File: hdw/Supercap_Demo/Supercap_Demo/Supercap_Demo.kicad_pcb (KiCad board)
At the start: 4 copper layers, 71 parts, among them J201 +3.3VIN, J202 VOUT, Q201 IRF7404, Q301 2N7002, Q401 2N7002, U301 LTC3128-UFD, U302 LTC4419DD, U401 LTC3129UD

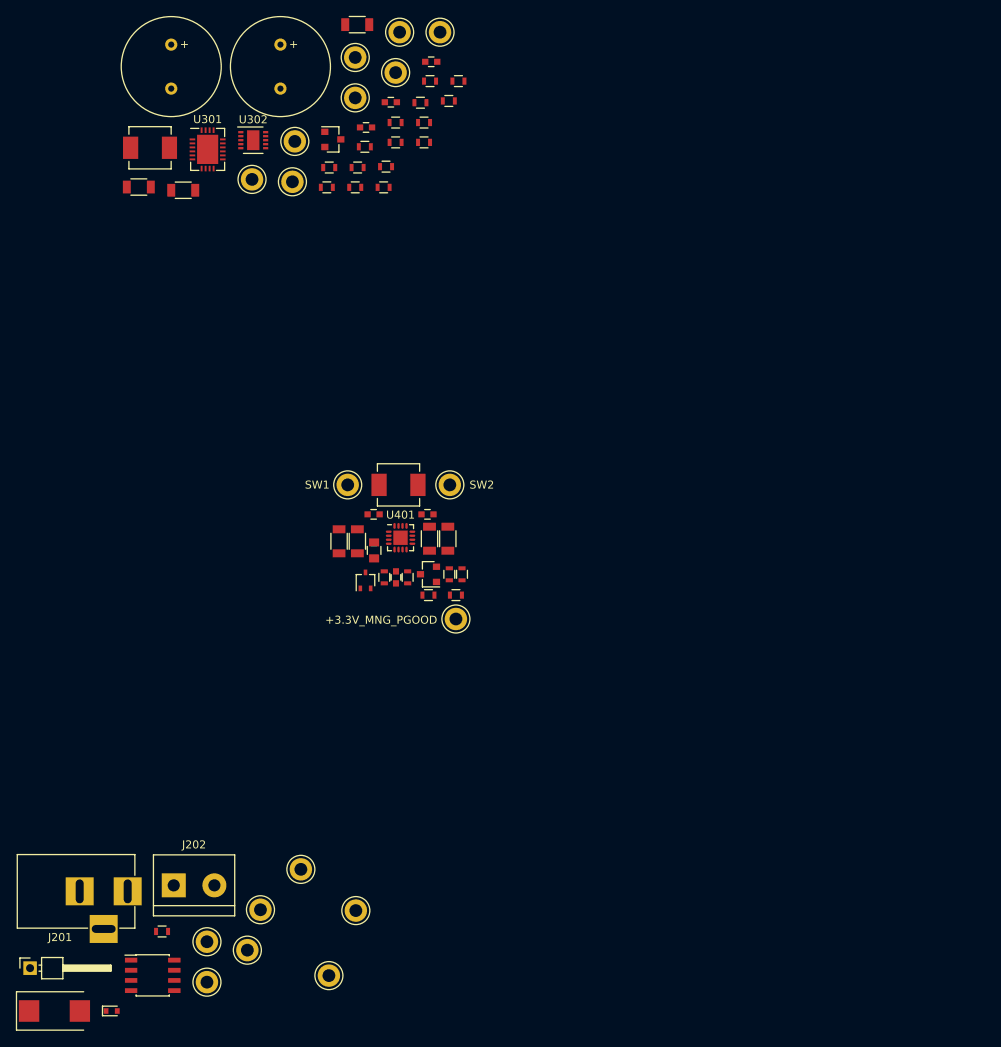
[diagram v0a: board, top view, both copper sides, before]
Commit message: Placed parts on PCB
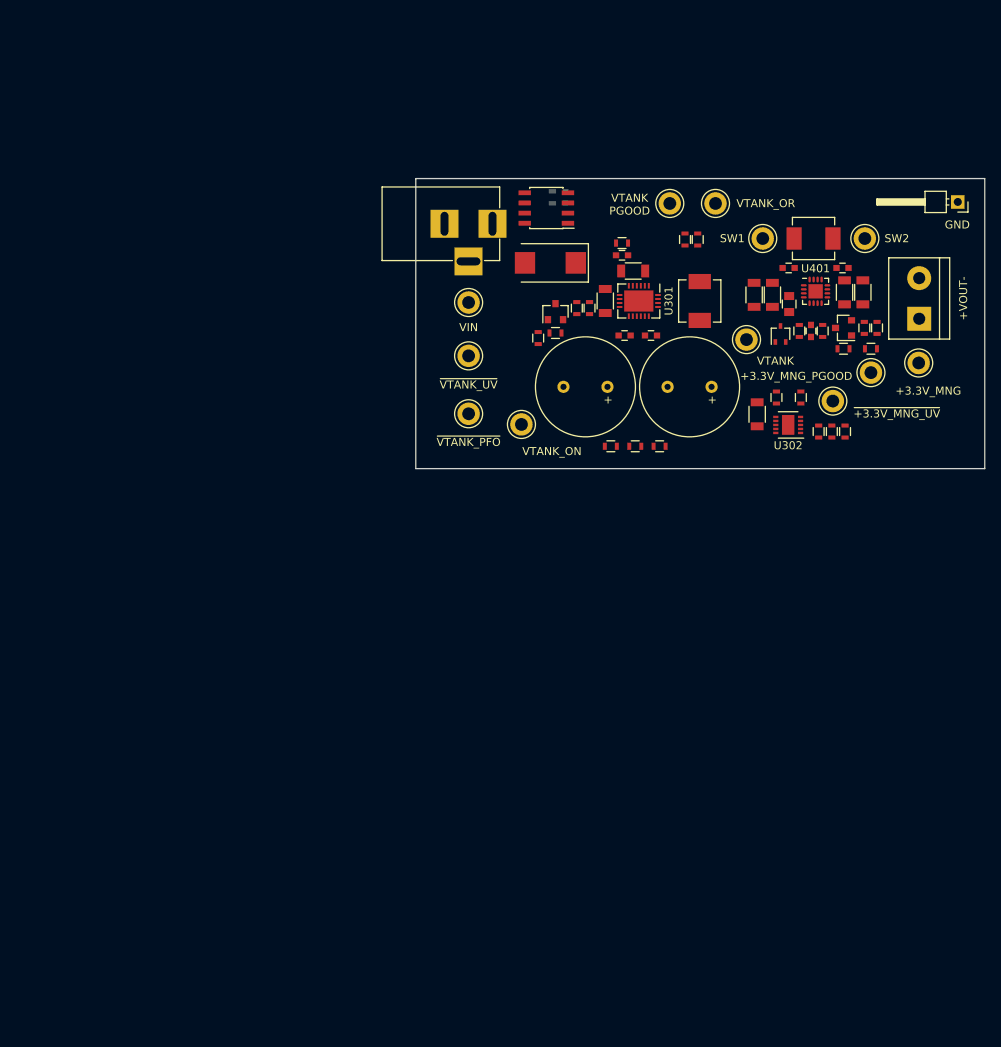
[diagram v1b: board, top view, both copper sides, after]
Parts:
- removed TP301, TP303, TP304, TP305, TP306, TP307: TP, Measurement_Points:Test_Point_Keystone_5005-5009_Compact
- D201, R201: moved to B.Cu
- moved TP202 150.4 mm to (172.0, 29.2), turned to 180 degrees
- moved J202 117.0 mm to (167.1, 43.8), turned to 90 degrees
- moved D201 116.5 mm to (122.9, 28.6), turned to 90 degrees
- moved C201 112.2 mm to (121.0, 36.8), turned to 180 degrees
- moved Q201 107.8 mm to (120.5, 30.0), turned to 180 degrees
- moved TP403 106.3 mm to (167.1, 49.3), turned to 270 degrees
- moved R201 103.9 mm to (121.3, 28.6), turned to 270 degrees
- moved TP201 96.7 mm to (136.0, 29.4), turned to 270 degrees
- moved J201 95.1 mm to (113.8, 31.9)
- moved TP204 88.6 mm to (156.3, 54.1), turned to 270 degrees
- moved TP208 85.5 mm to (110.8, 41.8), turned to 270 degrees
- moved TP206 80.0 mm to (117.4, 57.0), turned to 270 degrees
- moved U302 75.7 mm to (150.7, 57.1), turned to 180 degrees
- moved TP205 74.0 mm to (110.8, 48.5), turned to 270 degrees
- moved TP203 73.7 mm to (110.8, 55.7), turned to 270 degrees
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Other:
- board outline added: 71.1 x 36.3 mm
- board text added: "+3.3V_MNG"
- board text added: "+VOUT-"
- board text added: "GND"
- board text added: "VIN"
- board text added: "VTANK"
- board text added: "VTANK PGOOD"
- board text added: "VTANK_ON"
- board text added: "VTANK_OR"
- board text added: "~+3.3V_MNG_UV"
- board text added: "~VTANK_PFO"
- board text added: "~VTANK_UV"

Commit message: Placed parts on PCB
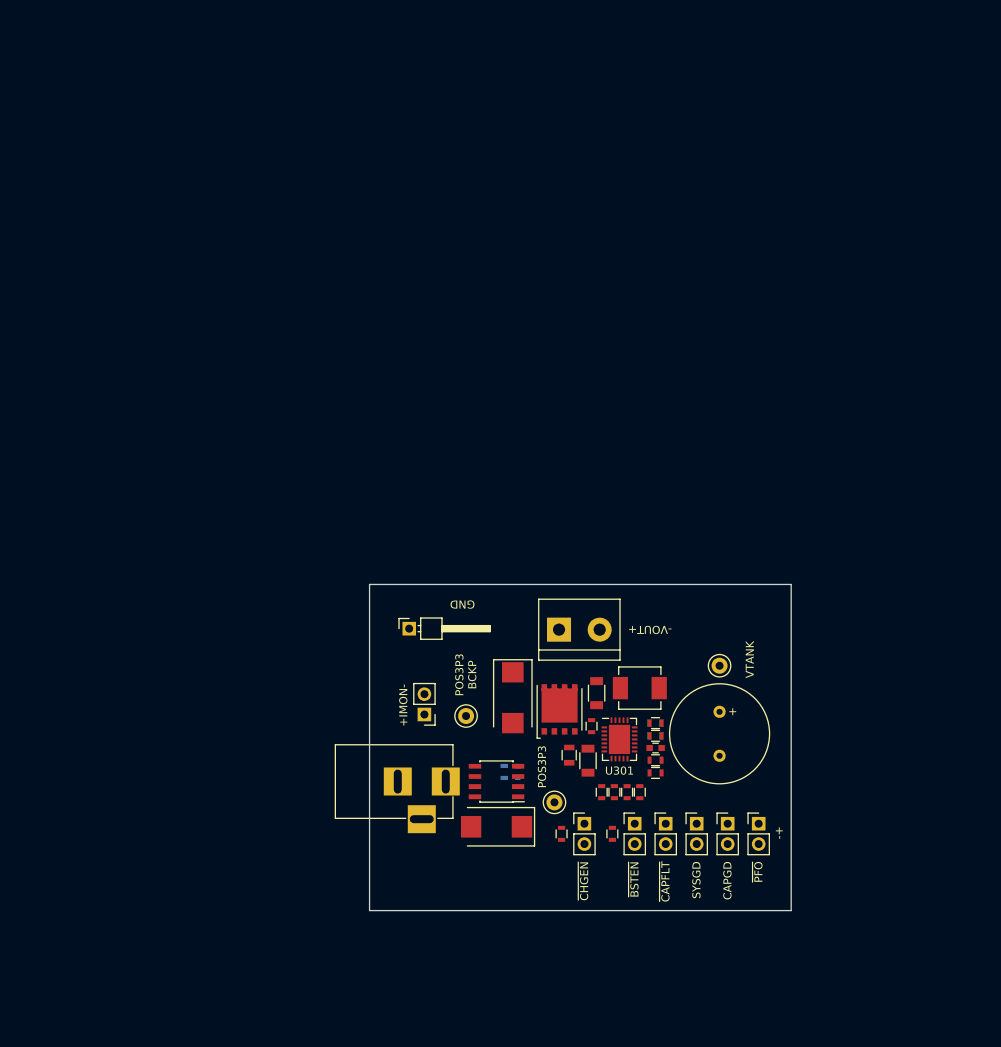
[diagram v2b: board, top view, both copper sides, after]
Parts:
- removed C306: 0.1uF, Capacitors_SMD:C_0603
- removed C307: 470pF, Capacitors_SMD:C_0603
- removed C308, C401, C402, C407, C408: 10uF, Capacitors_SMD:C_1206
- removed C403, C404: 22nF, Capacitors_SMD:C_0603
- removed C405: 2.2uF, Capacitors_SMD:C_0805
- removed C406: 33pF, Capacitors_SMD:C_0603
- removed D401: BAT54W, TO_SOT_Packages_SMD:SOT-323_SC-70
- removed L401: 3.3uH, Inductors_SMD:L_Vishay_IHLP-2020
- removed Q401: 2N7002, TO_SOT_Packages_SMD:SOT-23
- removed R315, R402, R404, R405: 1M, Resistors_SMD:R_0603
- removed R401: 10, Resistors_SMD:R_0603
- removed R403: 100k, Resistors_SMD:R_0603
- removed R406: 1.07M, Resistors_SMD:R_0603
- removed R407: 590k, Resistors_SMD:R_0603
- removed TP203, TP204, TP205, TP206, TP207, TP208, TP308, TP401, TP402, TP403: TP, Measurement_Points:Test_Point_Keystone_5005-5009_Compact
- removed U302: LTC4419DD, Housings_DFN_QFN:DFN-10-1EP_3x3mm_Pitch0.5mm
- removed U401: LTC3129UD, Housings_DFN_QFN:QFN-16-1EP_3x3mm_Pitch0.5mm
- added JP301: ~CHGEN, Pin_Headers:Pin_Header_Straight_1x02_Pitch2.54mm, F.Cu at (125.3, 106.9)
- added JP302: ~BSTEN, Pin_Headers:Pin_Header_Straight_1x02_Pitch2.54mm, F.Cu at (131.6, 106.9)
- added TP301: IMON, Pin_Headers:Pin_Header_Straight_1x02_Pitch2.54mm, F.Cu at (105.3, 93.3)
- added TP303: CAPGD, Pin_Headers:Pin_Header_Straight_1x02_Pitch2.54mm, F.Cu at (143.2, 106.9)
- added TP304: SYSGD, Pin_Headers:Pin_Header_Straight_1x02_Pitch2.54mm, F.Cu at (139.3, 106.9)
- added TP305: PFO, Pin_Headers:Pin_Header_Straight_1x02_Pitch2.54mm, F.Cu at (147.1, 106.9)
- added TP306: TP, Measurement_Points:Test_Point_Keystone_5000-5004_Miniature, F.Cu at (110.5, 93.5)
- added TP307: TP, Measurement_Points:Test_Point_Keystone_5000-5004_Miniature, F.Cu at (142.2, 87.2)
- C302: value 10uF -> 2.2nF; footprint Capacitors_SMD:C_1206 -> Capacitors_SMD:C_0603
- C303: value 15F -> 10uF; footprint Custom Footprints Library:SCCT30B156SRB -> Capacitors_SMD:C_1206
- C305: value 0.1uF -> 100uF; footprint Capacitors_SMD:C_0603 -> Capacitors_Tantalum_SMD:CP_Tantalum_Case-D_EIA-7343-31_Reflow
- L301: value 3.3uH -> 2.2uH
- Q301: value 2N7002 -> IPC100N04S51R7ATMA1; footprint TO_SOT_Packages_SMD:SOT-23 -> TO_SOT_Packages_SMD:TDSON-8-1
- R304: value 124k -> 1M
- R306: value 10 -> 1M
- R307: value 3.6k -> 121k; moved to B.Cu
- R308: value 2.2M -> 75k; moved to B.Cu
- R309: value 3.65k -> 12m; footprint Resistors_SMD:R_0603 -> Resistors_SMD:R_0805
- R310: value 340k -> 1k
- R311: value 1M -> 1.07M
- R312: value 324k -> 340k
- R313: value 276k -> 931k
- R314: value 1M -> 392k
- TP201: footprint Measurement_Points:Test_Point_Keystone_5005-5009_Compact -> Pin_Headers:Pin_Header_Angled_1x01_Pitch2.54mm
- TP202: footprint Pin_Headers:Pin_Header_Angled_1x01_Pitch2.54mm -> Measurement_Points:Test_Point_Keystone_5000-5004_Miniature
- TP302: value TP -> ~CAPFLT; footprint Measurement_Points:Test_Point_Keystone_5005-5009_Compact -> Pin_Headers:Pin_Header_Straight_1x02_Pitch2.54mm
- U301: value LTC3128-UFD -> LTC4041UFD; footprint Housings_DFN_QFN:QFN-20-1EP_4x5mm_Pitch0.5mm -> Housings_DFN_QFN:QFN-24-1EP_4x5mm_Pitch0.5mm
- moved TP202 90.4 mm to (121.5, 104.3), turned to 0 degrees
- moved R201 72.1 mm to (115.3, 100.5)
- moved D201 72.1 mm to (117.0, 100.5)
- moved Q201 72.0 mm to (114.3, 101.7)
- moved C201 70.8 mm to (114.3, 107.3)
- moved J201 70.0 mm to (108.0, 101.7)
- moved R302 69.6 mm to (129.0, 103.0)
- moved R304 65.8 mm to (122.4, 108.2)
- moved R301 65.3 mm to (134.2, 99.0), turned to 180 degrees
- moved R306 62.7 mm to (128.8, 108.2), turned to 90 degrees
- moved TP201 62.3 mm to (103.4, 82.5), turned to 0 degrees
- moved TP302 61.4 mm to (135.4, 106.9), turned to 0 degrees
- moved R307 60.2 mm to (134.2, 94.4), turned to 180 degrees
- moved C302 59.7 mm to (134.2, 97.5), turned to 0 degrees
- moved J202 59.5 mm to (122.1, 82.7), turned to 0 degrees
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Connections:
- C303 pad 1: VTANK -> +3.3V_BCKP
- C303 pad 2: Net-(C303-Pad2) -> GND
- C304 pad 1: Net-(C303-Pad2) -> VTANK
- C305 pad 1: VTANK -> +3.3V_BCKP
- C305 pad 2: Net-(C303-Pad2) -> GND
- J202 pad 1: +3.3V_MNG -> +3.3V_BCKP
- L301 pad 2: Net-(L301-Pad2) -> VTANK
- Q301 pad 2: GND -> Net-(Q301-Pad1)
- Q301 pad 3: Net-(Q301-Pad3) -> Net-(Q301-Pad1)
- R301 pad 1: ~TANK_PFO -> +3.3V_BCKP
- R301 pad 2: +3.3V_MNG -> ~BCKP_PFO
- R302 pad 1: TANK_PGOOD -> +3.3V_BCKP
- R302 pad 2: +3.3V_MNG -> BCKP_SYSGD
- R303 pad 1: Net-(Q301-Pad3) -> +3.3V_BCKP
- R303 pad 2: +3V3 -> BCKP_CAPGD
- R304 pad 1: GND -> +3V3
- R304 pad 2: Net-(R304-Pad2) -> Net-(JP301-Pad1)
- R305 pad 1: GND -> +3.3V_BCKP
- R305 pad 2: Net-(Q301-Pad1) -> ~BCKP_CAPFLT
- R306 pad 1: Net-(Q301-Pad1) -> +3V3
- R306 pad 2: VTANK_ON -> Net-(JP302-Pad1)
- R307 pad 1: GND -> +3V3
- R307 pad 2: Net-(C307-Pad1) -> Net-(R307-Pad2)
- R308 pad 1: Net-(R308-Pad1) -> Net-(R307-Pad2)
- R308 pad 2: VTANK -> GND
- R309 pad 1: Net-(R309-Pad1) -> Net-(Q301-Pad1)
- R309 pad 2: Net-(R308-Pad1) -> +3V3
- R310 pad 1: GND -> Net-(R310-Pad1)
- R310 pad 2: Net-(R309-Pad1) -> GND
- R311 pad 1: Net-(R311-Pad1) -> +3.3V_BCKP
- R311 pad 2: Net-(C302-Pad1) -> Net-(R311-Pad2)
- R312 pad 1: Net-(R312-Pad1) -> Net-(R311-Pad2)
- R312 pad 2: Net-(R311-Pad1) -> GND
- R313 pad 1: GND -> VTANK
- R313 pad 2: Net-(R312-Pad1) -> Net-(R313-Pad2)
- R314 pad 1: ~POS3P3_UV -> Net-(R313-Pad2)
- R314 pad 2: +3.3V_MNG -> GND
- TP201 pad 1: TANK_PGOOD -> GND
- TP202 pad 1: GND -> +3V3
- TP302 pad 1: VTANK -> ~BCKP_CAPFLT
- U301 pad 1: Net-(L301-Pad2) -> +3.3V_BCKP
- U301 pad 10: Net-(R304-Pad2) -> Net-(R311-Pad2)
- U301 pad 11: Net-(R308-Pad1) -> BCKP_SYSGD
- U301 pad 12: TANK_PGOOD -> Net-(R313-Pad2)
- U301 pad 13: Net-(C303-Pad2) -> BCKP_CAPGD
- U301 pad 14: VTANK -> ~BCKP_PFO
- U301 pad 15: VTANK -> Net-(Q301-Pad4)
- U301 pad 16: VTANK -> +3V3
- U301 pad 17: Net-(L301-Pad1) -> Net-(C302-Pad1)
- U301 pad 18: Net-(L301-Pad1) -> Net-(R311-Pad2)
- U301 pad 19: Net-(L301-Pad2) -> Net-(R307-Pad2)
- U301 pad 2: Net-(C302-Pad1) -> Net-(R310-Pad1)
- U301 pad 20: (no net) -> GND
- U301 pad 21: GND -> Net-(L301-Pad1)
- U301 pad 3: Net-(C302-Pad1) -> BCKP_IMON
- U301 pad 4: Net-(Q301-Pad3) -> Net-(JP301-Pad1)
- U301 pad 5: Net-(C307-Pad1) -> Net-(JP302-Pad1)
- U301 pad 6: (no net) -> +3V3
- U301 pad 7: +3V3 -> Net-(Q301-Pad1)
- U301 pad 8: ~TANK_PFO -> ~BCKP_CAPFLT
- U301 pad 9: Net-(Q301-Pad3) -> (no net)
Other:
- board size 71.1 x 36.3 mm -> 52.7 x 40.8 mm
- board text added: "+IMON-"
- board text added: "-+"
- board text added: "-VOUT+"
- board text added: "CAPGD"
- board text added: "POS3P3"
- board text added: "POS3P3 BCKP"
- board text added: "SYSGD"
- board text added: "~BSTEN"
- board text added: "~CAPFLT"
- board text added: "~CHGEN"
- board text added: "~PFO"
- board text removed: "+3.3V_MNG"
- board text removed: "+3.3V_MNG_PGOOD"
- board text removed: "+VOUT-"
- board text removed: "SW1"
- board text removed: "SW2"
- board text removed: "VIN"
- board text removed: "VTANK PGOOD"
- board text removed: "VTANK_ON"
- board text removed: "VTANK_OR"
- board text removed: "~+3.3V_MNG_UV"
- board text removed: "~VTANK_PFO"
- board text removed: "~VTANK_UV"

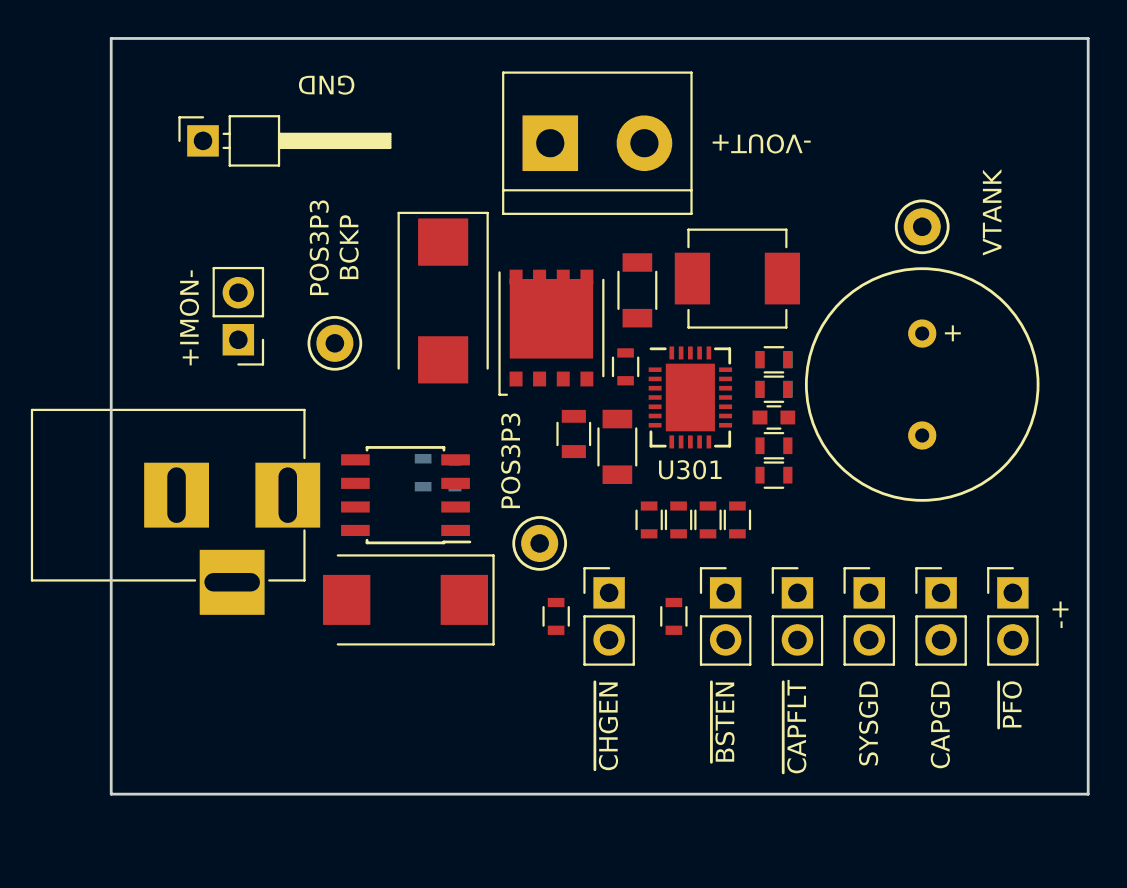
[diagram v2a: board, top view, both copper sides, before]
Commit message: Routed board
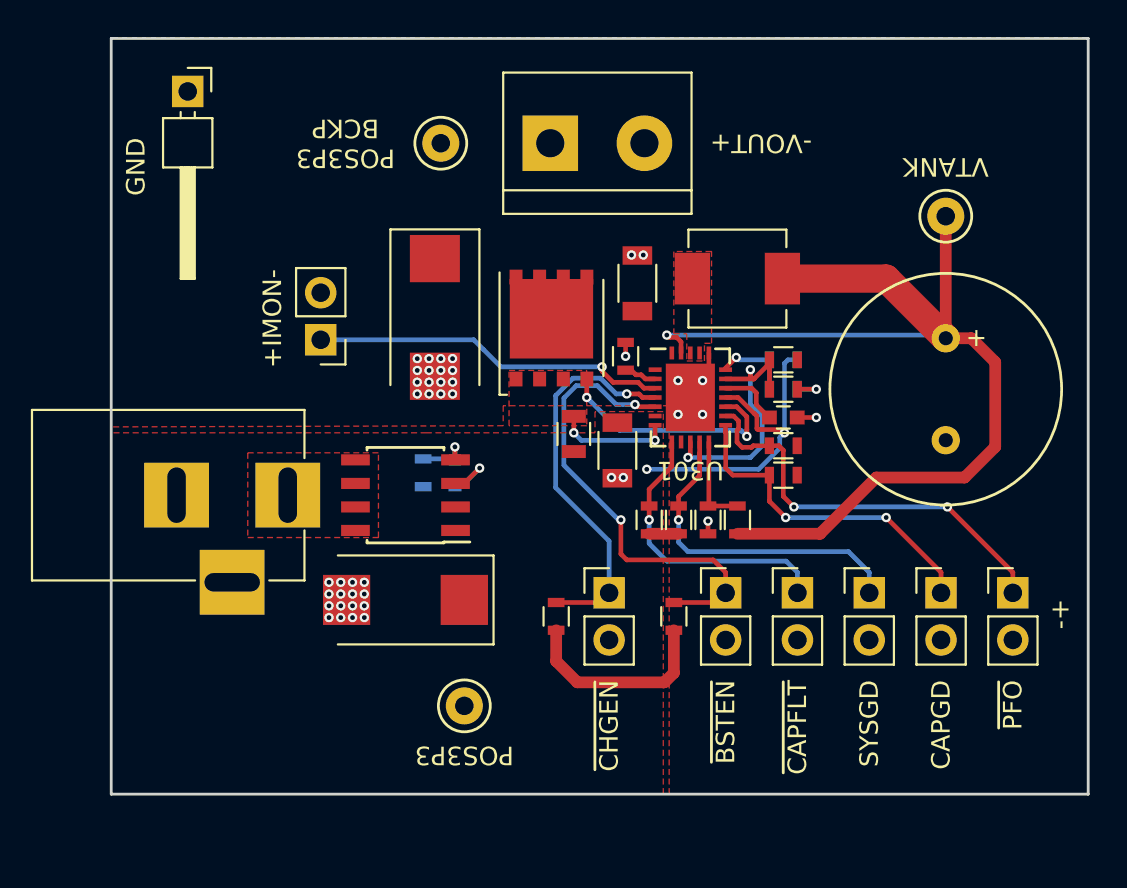
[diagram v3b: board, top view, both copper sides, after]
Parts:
- moved TP306 12.2 mm to (116.2, 82.7)
- moved TP202 9.66 mm to (117.5, 113.0)
- moved TP301 4.44 mm to (109.7, 93.3)
- moved TP201 2.79 mm to (102.6, 79.9), turned to 270 degrees
- moved TP307 1.39 mm to (143.4, 86.6)
- moved C304 1.30 mm to (143.4, 95.9)
- moved C305 0.99 mm to (115.9, 92.1)
- moved R310 0.57 mm to (126.2, 94.2)
- moved C302 0.51 mm to (134.7, 97.5)
- moved R301 0.51 mm to (134.7, 99.0)
- moved R303 0.51 mm to (134.7, 100.6)
- moved R307 0.51 mm to (134.7, 94.4)
- moved R308 0.51 mm to (134.7, 95.9)
- moved R311 0.51 mm to (134.7, 94.4)
- moved R312 0.51 mm to (134.7, 95.9)
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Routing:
- net VTANK: track 0.00 -> 57.0 mm, vias 0 -> 1
- net +3V3: track 0.00 -> 31.8 mm, vias 0 -> 3
- net Net-(JP302-Pad1): track 0.00 -> 25.6 mm, vias 0 -> 2
- net ~BCKP_PFO: track 0.00 -> 22.4 mm, vias 0 -> 2
- net Net-(JP301-Pad1): track 0.00 -> 21.1 mm, vias 0 -> 1
- net BCKP_IMON: track 0.00 -> 19.3 mm, vias 0 -> 1
- net BCKP_CAPGD: track 0.00 -> 18.2 mm, vias 0 -> 2
- net BCKP_SYSGD: track 0.00 -> 17.9 mm, vias 0 -> 1
- net ~BCKP_CAPFLT: track 0.00 -> 15.7 mm, vias 0 -> 1
- net Net-(R311-Pad2): track 0.00 -> 14.6 mm, vias 0 -> 2
- net Net-(Q301-Pad4): track 0.00 -> 12.9 mm, vias 0 -> 2
- net Net-(Q301-Pad1): track 0.00 -> 6.25 mm, vias 0 -> 2
- net GND: track 0.00 -> 6.15 mm, vias 0 -> 44
- net Net-(R313-Pad2): track 0.00 -> 5.06 mm
- net Net-(R307-Pad2): track 0.00 -> 4.33 mm, vias 0 -> 1
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- added copper zone on F.Cu, net +3.3V_BCKP
- added copper zone on F.Cu, net +3V3
- added copper zone on B.Cu, net GND
- added copper zone on F.Cu, net Net-(J201-Pad1)
- added copper zone on F.Cu, net Net-(L301-Pad1)
- added copper zone on F.Cu, net Net-(Q301-Pad1)
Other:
- copper layers 4 -> 2
- net class Default: via_dia 0.8 -> 0.508; via_drill 0.4 -> 0.254
- net class Power: clearance 0.127 -> 0.1524; via_dia 0.5588 -> 0.508; via_drill 0.199898 -> 0.254
- net class Signal: clearance 0.127 -> 0.1524; via_dia 0.5588 -> 0.508; via_drill 0.199898 -> 0.254
